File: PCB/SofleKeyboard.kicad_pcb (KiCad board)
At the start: 2 copper layers, 137.5 x 109.3 mm, 85 parts, among them J1 LED, J2 4PIN, J3 OLED, P1 i2c_pin, P2 i2c_pin, SW1 SW_PUSH, SW10 SW_PUSH, SW11 SW_PUSH, SW12 SW_PUSH, SW13 SW_PUSH, SW14 SW_PUSH, SW15 SW_PUSH, SW16 SW_PUSH, SW17 SW_PUSH, SW18 SW_PUSH, SW19 SW_PUSH, SW2 SW_PUSH, SW20 SW_PUSH, SW21 SW_PUSH, SW22 SW_PUSH, SW23 SW_PUSH, SW24 SW_PUSH, SW25 Rotary_Encoder_Switch, SW26 SW_PUSH, SW27 SW_PUSH, SW28 SW_PUSH, SW29 SW_PUSH, SW3 SW_PUSH, SW30 SW_PUSH, SW4 SW_PUSH, SW5 SW_PUSH, SW6 SW_PUSH, SW7 SW_PUSH, SW8 SW_PUSH, SW9 SW_PUSH, U1 ProMicro

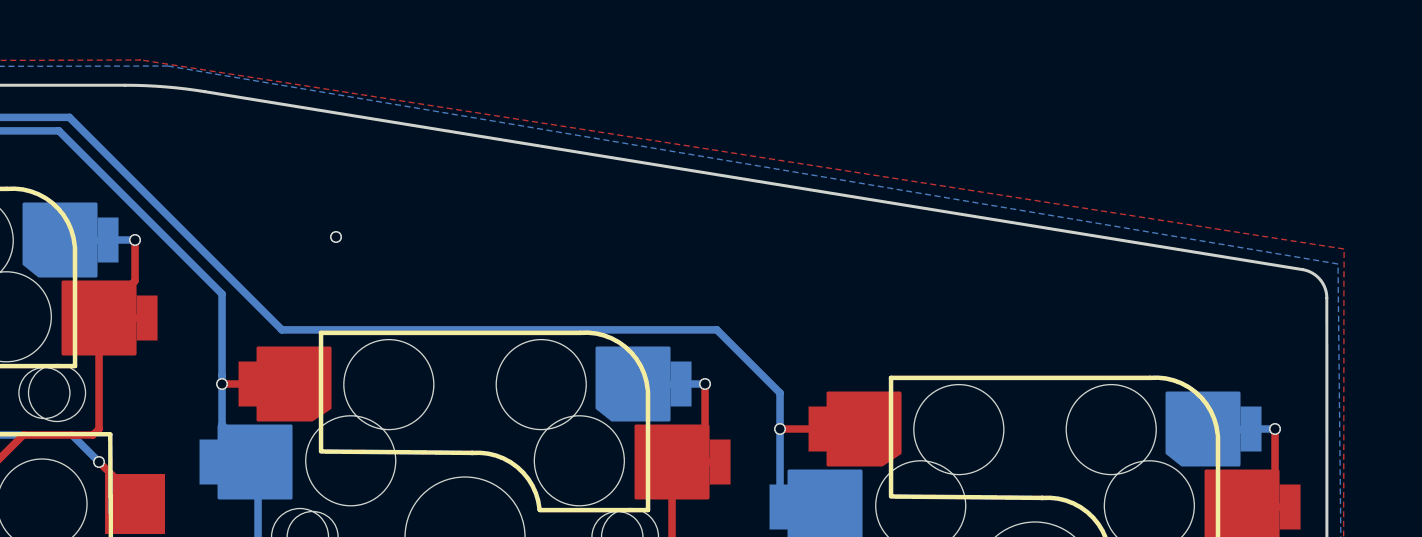
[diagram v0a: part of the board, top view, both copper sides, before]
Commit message: Add name to the PCB
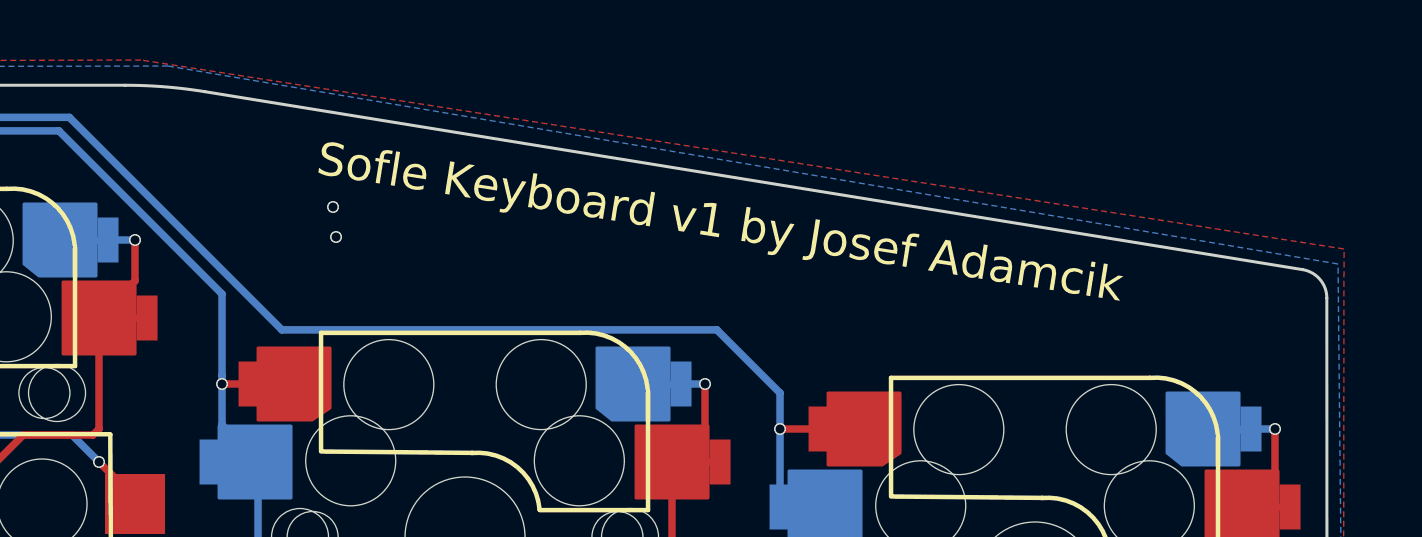
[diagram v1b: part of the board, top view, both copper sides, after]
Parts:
- J2: footprint SofleKeyboard-footprint:MJ-4PP-9_rev3 -> SofleKeyboard-footprint:MJ-4PP-9
- U1: footprint SofleKeyboard-footprint:ProMicro_rev2 -> SofleKeyboard-footprint:ProMicro
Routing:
- net (no net): vias 0 -> 1
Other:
- board text added: "Sofle Keyboard v1 by Josef Adamcik"

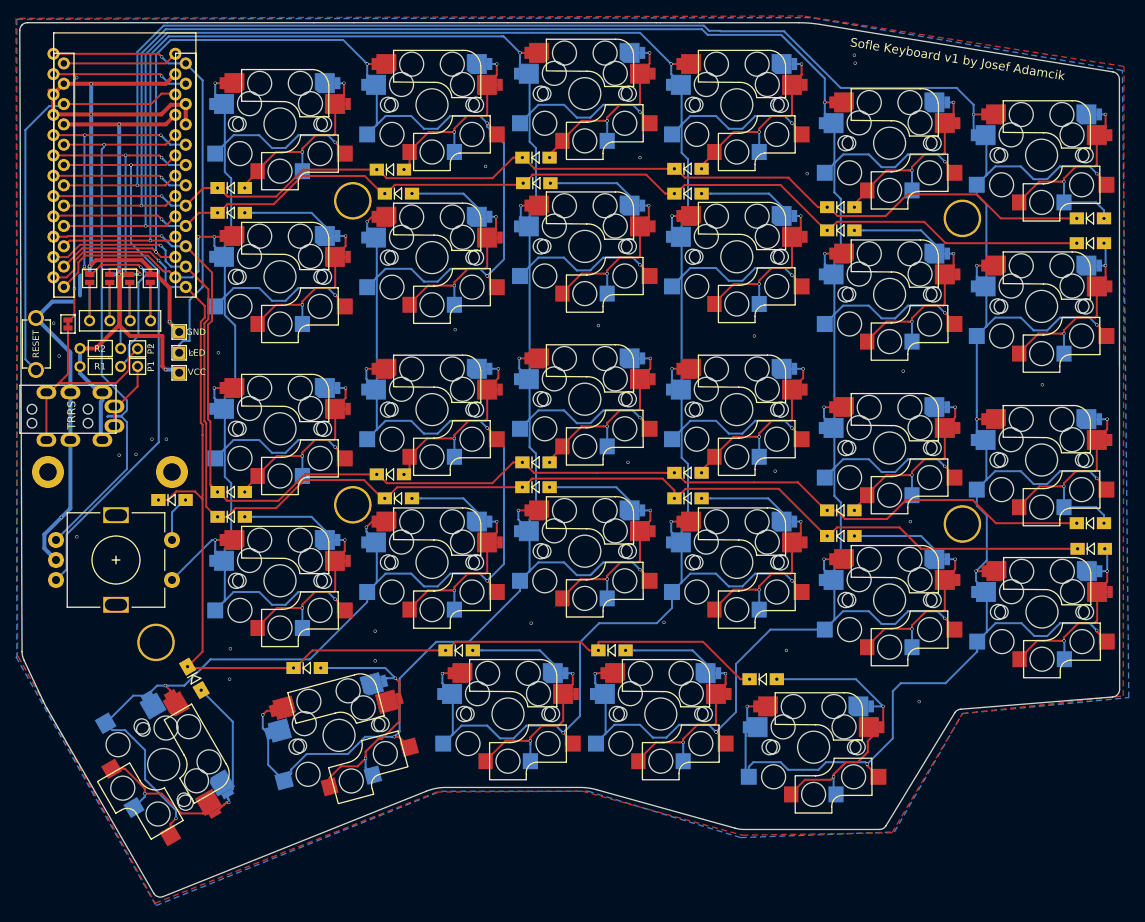
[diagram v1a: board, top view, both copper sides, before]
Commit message: Update the edge.cuts layer of the main pcb with current shape.
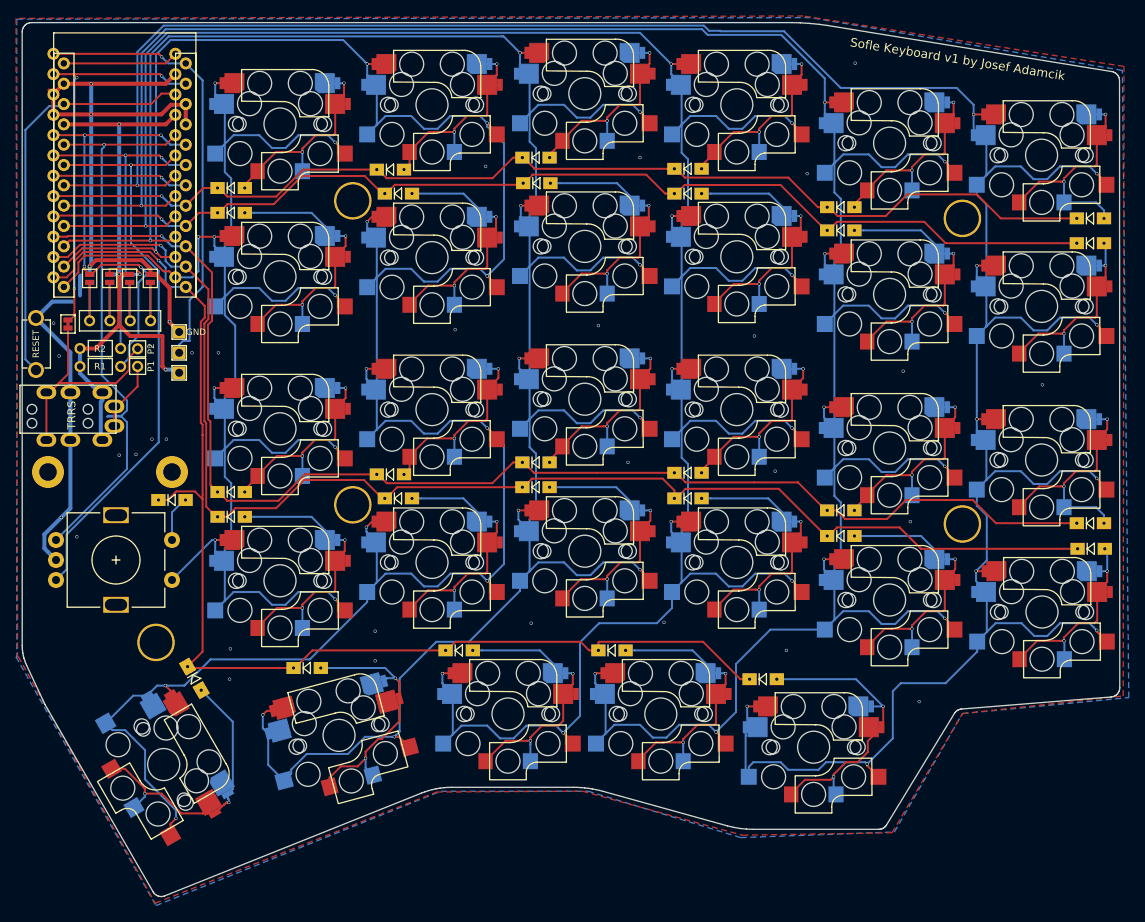
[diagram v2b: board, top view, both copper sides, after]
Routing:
- net (no net): vias 1 -> 0
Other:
- board size 137.5 x 109.3 mm -> 137.2 x 109.2 mm

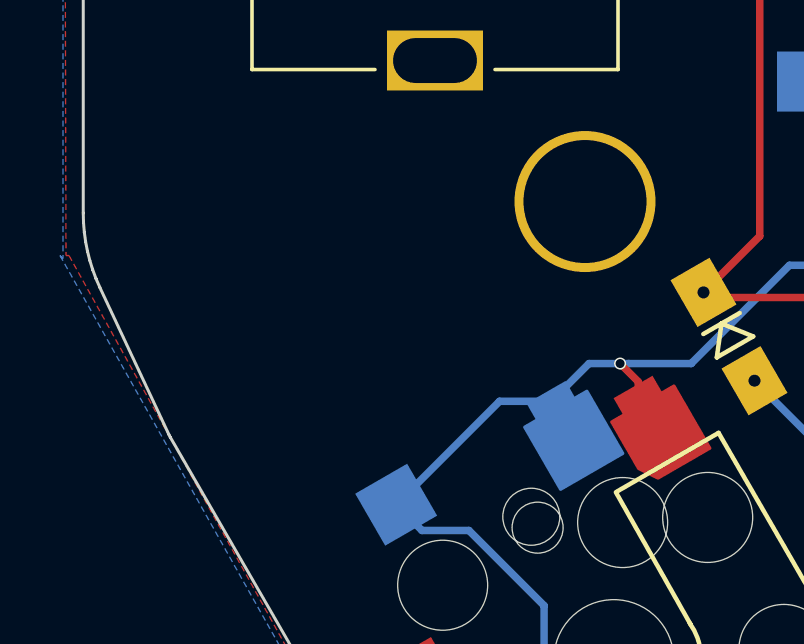
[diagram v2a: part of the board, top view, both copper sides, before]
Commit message: Add a small logo to main pcb
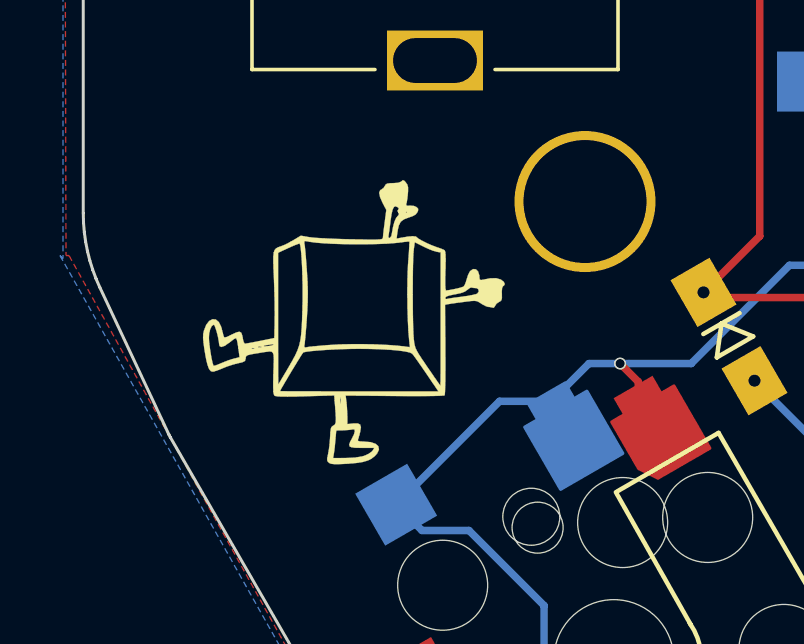
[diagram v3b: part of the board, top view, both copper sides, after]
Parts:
- added Ref**: Val**, SofleKeyboard-footprint:SofleLogoSmall, B.Cu at (96.6, 125.7)
- added Ref**: Val**, SofleKeyboard-footprint:SofleLogoSmall, F.Cu at (97.9, 125.9)

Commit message: Small details.
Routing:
- net GND: vias 36 -> 45
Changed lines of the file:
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@@
     (thickness 1.6)
     (drawings 193)
-    (tracks 1881)
+    (tracks 1892)
     (zones 0)
     (modules 87)
@@
   (layers
     (0 F.Cu signal)
-    (31 B.Cu signal hide)
+    (31 B.Cu signal)
     (32 B.Adhes user hide)
     (33 F.Adhes user hide)
@@
       (usegerberadvancedattributes false)
       (creategerberjobfile false)
-      (excludeedgelayer false)
+      (excludeedgelayer true)
       (linewidth 0.100000)
       (plotframeref true)
@@
   (gr_line (start 49.676679 -38.227998) (end 49.676679 -38.227998) (layer Edge.Cuts) (width 0.1))
   (gr_line (start 45.503294 -44.952764) (end 45.503294 -44.952764) (layer Eco2.User) (width 0.1))
+  (via (at 177.64 97.49) (size 0.4) (drill 0.3) (layers F.Cu B.Cu) (net 34))
   (segment (start 116.1 57.6) (end 116.1 58) (width 0.25) (layer F.Cu) (net 1) (status 30))
   (segment (start 117.7 56) (end 116.1 57.6) (width 0.25) (layer F.Cu) (net 1) (status 30))
@@
   (segment (start 202.3 104.32) (end 202.4 104.42) (width 0.25) (layer B.Cu) (net 28) (status 30))
   (segment (start 202.3 103.17) (end 202.3 104.32) (width 0.25) (layer B.Cu) (net 28) (status 30))
-  (segment (start 200.63 101.5) (end 202.3 103.17) (width 0.25) (layer B.Cu) (net 28) (status 20))
-  (segment (start 192.3 101.5) (end 200.63 101.5) (width 0.25) (layer B.Cu) (net 28) (status 10))
   (segment (start 203.88 104.42) (end 203.9 104.4) (width 0.25) (layer B.Cu) (net 28) (status 30))
   (segment (start 202.4 104.42) (end 203.88 104.42) (width 0.25) (layer B.Cu) (net 28) (status 30))
+  (segment (start 193.145 102.195) (end 201.325 102.195) (width 0.25) (layer B.Cu) (net 28))
+  (segment (start 192.45 101.5) (end 193.145 102.195) (width 0.25) (layer B.Cu) (net 28))
+  (segment (start 192.3 101.5) (end 192.45 101.5) (width 0.25) (layer B.Cu) (net 28))
+  (segment (start 201.325 102.195) (end 202.3 103.17) (width 0.25) (layer B.Cu) (net 28))
   (via (at 218.5 114.599992) (size 0.4) (drill 0.3) (layers F.Cu B.Cu) (net 29))
   (segment (start 215.150008 114.599992) (end 218.075736 114.599992) (width 0.25) (layer F.Cu) (net 29))
@@
   (via (at 114.2 119.4) (size 0.4) (drill 0.3) (layers F.Cu B.Cu) (net 34))
   (via (at 132.4 117.1) (size 0.4) (drill 0.3) (layers F.Cu B.Cu) (net 34))
+  (via (at 184.42 95.59) (size 0.4) (drill 0.3) (layers F.Cu B.Cu) (net 34))
+  (via (at 182.82 96.87) (size 0.4) (drill 0.3) (layers F.Cu B.Cu) (net 34))
+  (via (at 210.46 98.43) (size 0.4) (drill 0.3) (layers F.Cu B.Cu) (net 34))
+  (via (at 210.5 101.7) (size 0.4) (drill 0.3) (layers F.Cu B.Cu) (net 34))
+  (via (at 207.81 64.34) (size 0.4) (drill 0.3) (layers F.Cu B.Cu) (net 34))
+  (via (at 214.66 63.35) (size 0.4) (drill 0.3) (layers F.Cu B.Cu) (net 34))
+  (via (at 173.08 115.59) (size 0.4) (drill 0.3) (layers F.Cu B.Cu) (net 34))
+  (via (at 196.55 101.11) (size 0.4) (drill 0.3) (layers F.Cu B.Cu) (net 34))
   (segment (start 106.17 57.67) (end 107.47 56.37) (width 0.25) (layer F.Cu) (net 35) (status 20))
   (segment (start 106.165745 57.665745) (end 106.17 57.67) (width 0.25) (layer F.Cu) (net 35))
